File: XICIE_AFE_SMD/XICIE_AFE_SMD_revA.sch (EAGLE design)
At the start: 21 parts, among them IC1 LM324D, IC2 CY8C4245T, IC3 AAT1217, J1 22-27-2021-02, Q1 MOSFET-NCHANNELBSS123LT1G, Q2 MOSFET-NCHANNELBSS123LT1G

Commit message: Trying to merge display
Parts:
- removed R8: 1.02 M, rcl:R-EU_R0805
- removed R9: 604 K, rcl:R-EU_R0603
- added C4, C5, C6, C7: 1 uF, rcl:C-EUC0402
- added C8: 2.2 uF, rcl:C-EUC0603
- added C9: 4.7 uF, rcl:C-EUC0603
- added R5: 390K, resistor:R-EU_R0603
- added U$2: ER-OLED0.96, juliano:ER-OLED0.96
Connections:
- removed net N$14: IC3.FB, R8.2, R9.1
- new net C1N: C4.1, U$2G$5.1
- new net C1P: C4.2, U$2G$4.1
- new net C2N: C5.1, U$2G$3.1
- new net C2P: C5.2, U$2G$2.1
- new net CS#: U$2G$13.1
- new net D/C#: U$2G$15.1
- new net D0: U$2G$18.1
- new net D1: U$2G$19.1
- new net D2: U$2G$20.1
- new net D3: U$2G$21.1
- new net D4: U$2G$22.1
- new net D5: U$2G$23.1
- new net D6: U$2G$24.1
- new net D7: U$2G$25.1
- new net E/RD#: U$2G$17.1
- new net IREF: R5.1, U$2G$26.1
- new net N.C.: U$2G$7.1
- new net R/W#: U$2G$16.1
- new net RES#: U$2G$14.1
- new net V+: C6.1, U$2G$6.1
- new net V2.1: C9.1, U$2G$27.1
- new net VCC_DISPLAY: C8.1, U$2G$28.1
- new net VDD: C7.1, U$2G$11.1, U$2G$9.1
- net GND: now also C6.2, C7.2, C8.2, C9.2, R5.2, U$2G$1.1, U$2G$10.1, U$2G$12.1, U$2G$29.1, U$2G$30.1, U$2G$8.1; no longer R9.2
- net VCC: no longer R8.1
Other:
- note added: "1.65 - 3.3"
- note added: "3.5 - 4.2"
- note added: "BS0"
- note added: "BS1"
- note added: "BS2"
- note added: "Fixed Voltage Must be unconnected"
- note added: "N.C.(GND)"
- note added: "VBAT"
- note added: "VCOMH"
- note added: "VLSS"
- note added: "VSS"

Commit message: Intermediate commit to change computers...
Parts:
- added R7: 1.02 M, rcl:R-EU_R0805
- added R8: 604 k, rcl:R-EU_R0603
- added R9: 150 k, rcl:R-EU_R0603
- added U$3: AAT3221, juliano:AAT3221
- added U$4: MMA7660FC, juliano:MMA7660FC
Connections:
- removed net D0: U$2G$18.1
- removed net D1: U$2G$19.1
- removed net D2: U$2G$20.1
- removed net V+: C6.1, U$2G$6.1
- removed net VDD: C7.1, U$2G$11.1, U$2G$9.1
- new net +3V3: C3.1, C6.1, D1.C, IC1P.V+, IC2.VDDDA, IC3.VOUT, R2.2, R3.2, R7.1, R9.1, U$1.C, U$2G$6.1, U$3.IN, U$4.AVDD
- new net N$12: IC3.FB, R7.2, R8.1
- new net N$14: R9.2, U$3.EN
- new net SCL: U$2G$18.1, U$4.SCL
- new net SDA: U$2G$19.1, U$2G$20.1, U$4.SDA
- net GND: now also R8.2, U$3.GND, U$4.AVSS, U$4.DVSS, U$4.RESERVED(GND)
- net VCC: now also C7.1, IC2.VCCD, IC2.VDDD(19), IC2.VDDD(34), U$2G$11.1, U$2G$9.1, U$3.OUT, U$4.DVDD; no longer C3.1, D1.C, IC1P.V+, IC2.VDDDA, IC3.VOUT, R2.2, R3.2, U$1.C
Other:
- note added: "1.8V"
- note added: "D0"
- note added: "D1"
- note added: "D2"
- note added: "RECALCULAR"
- note added: "SA0"
- note added: "SCL"
- note added: "SDA"
- note added: "VDD"
- note removed: "Fixed Voltage Must be unconnected"
- moved on the sheet: C3, R4

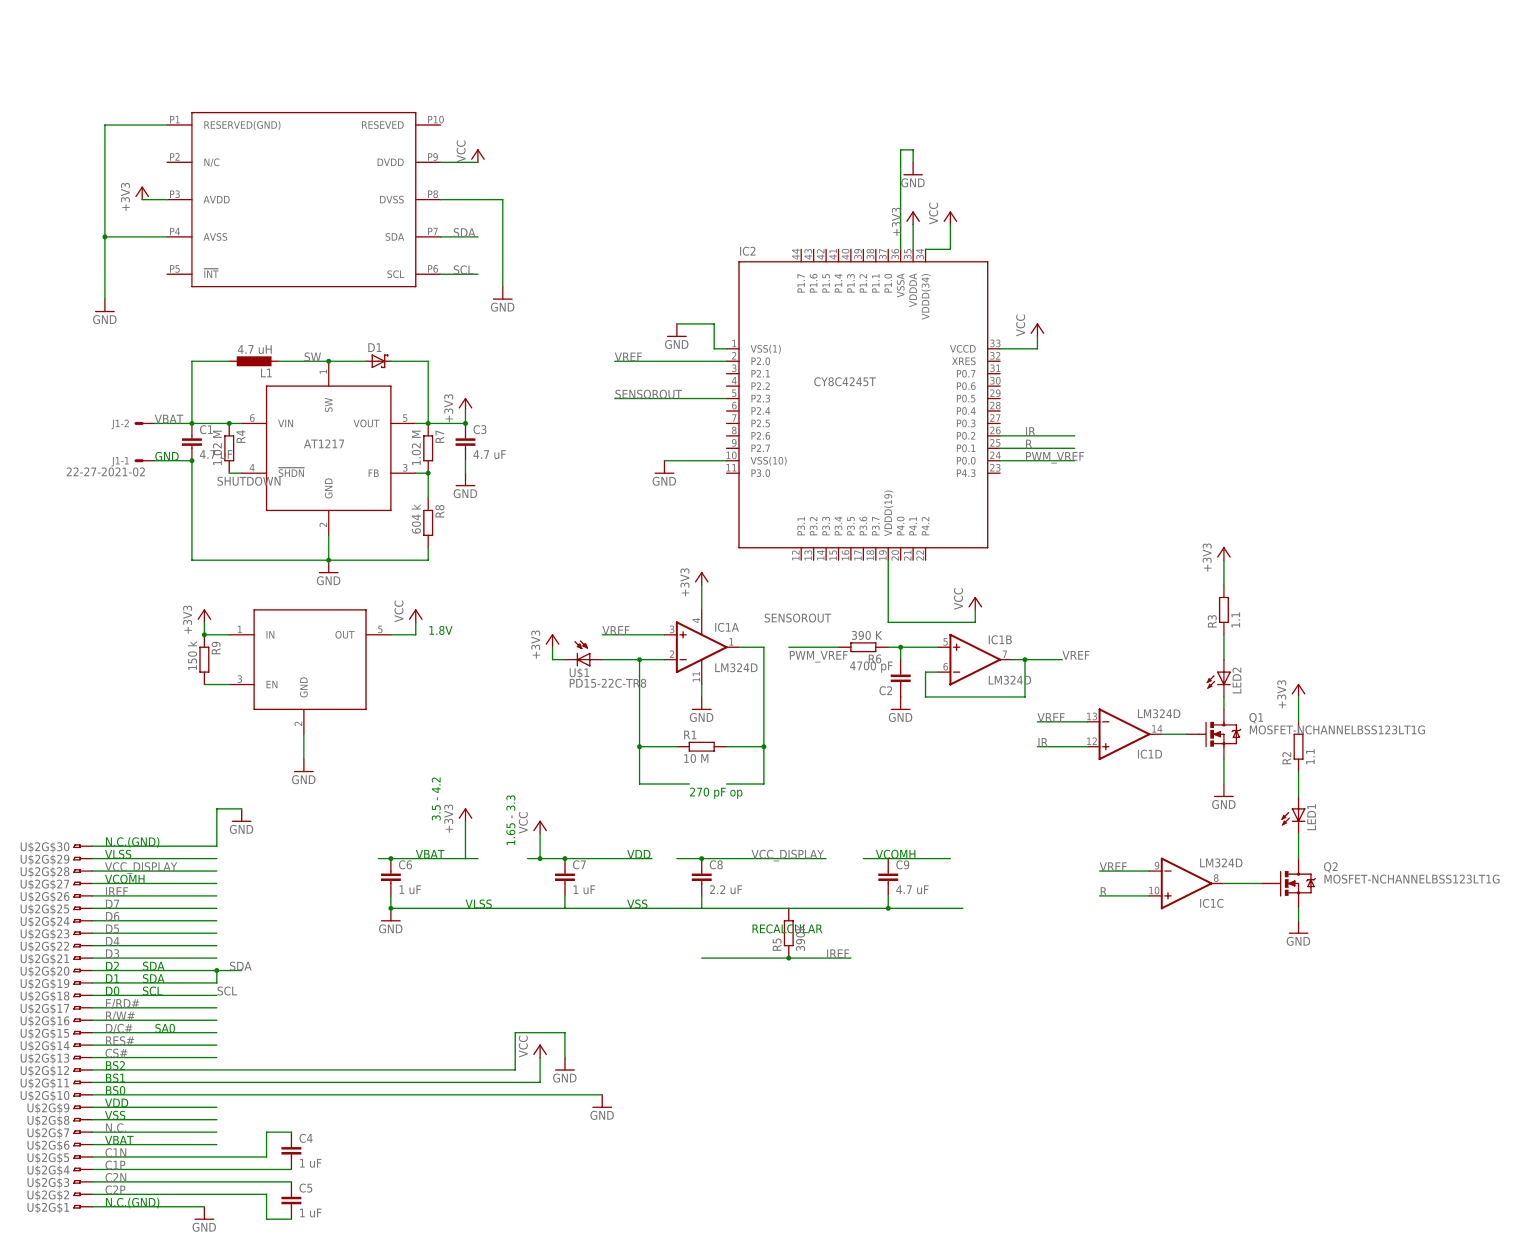
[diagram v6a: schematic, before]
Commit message: Added all components and connections
Still in doubt if BUZZ driver will use a resistor,
and if TIA should have a capacitor.
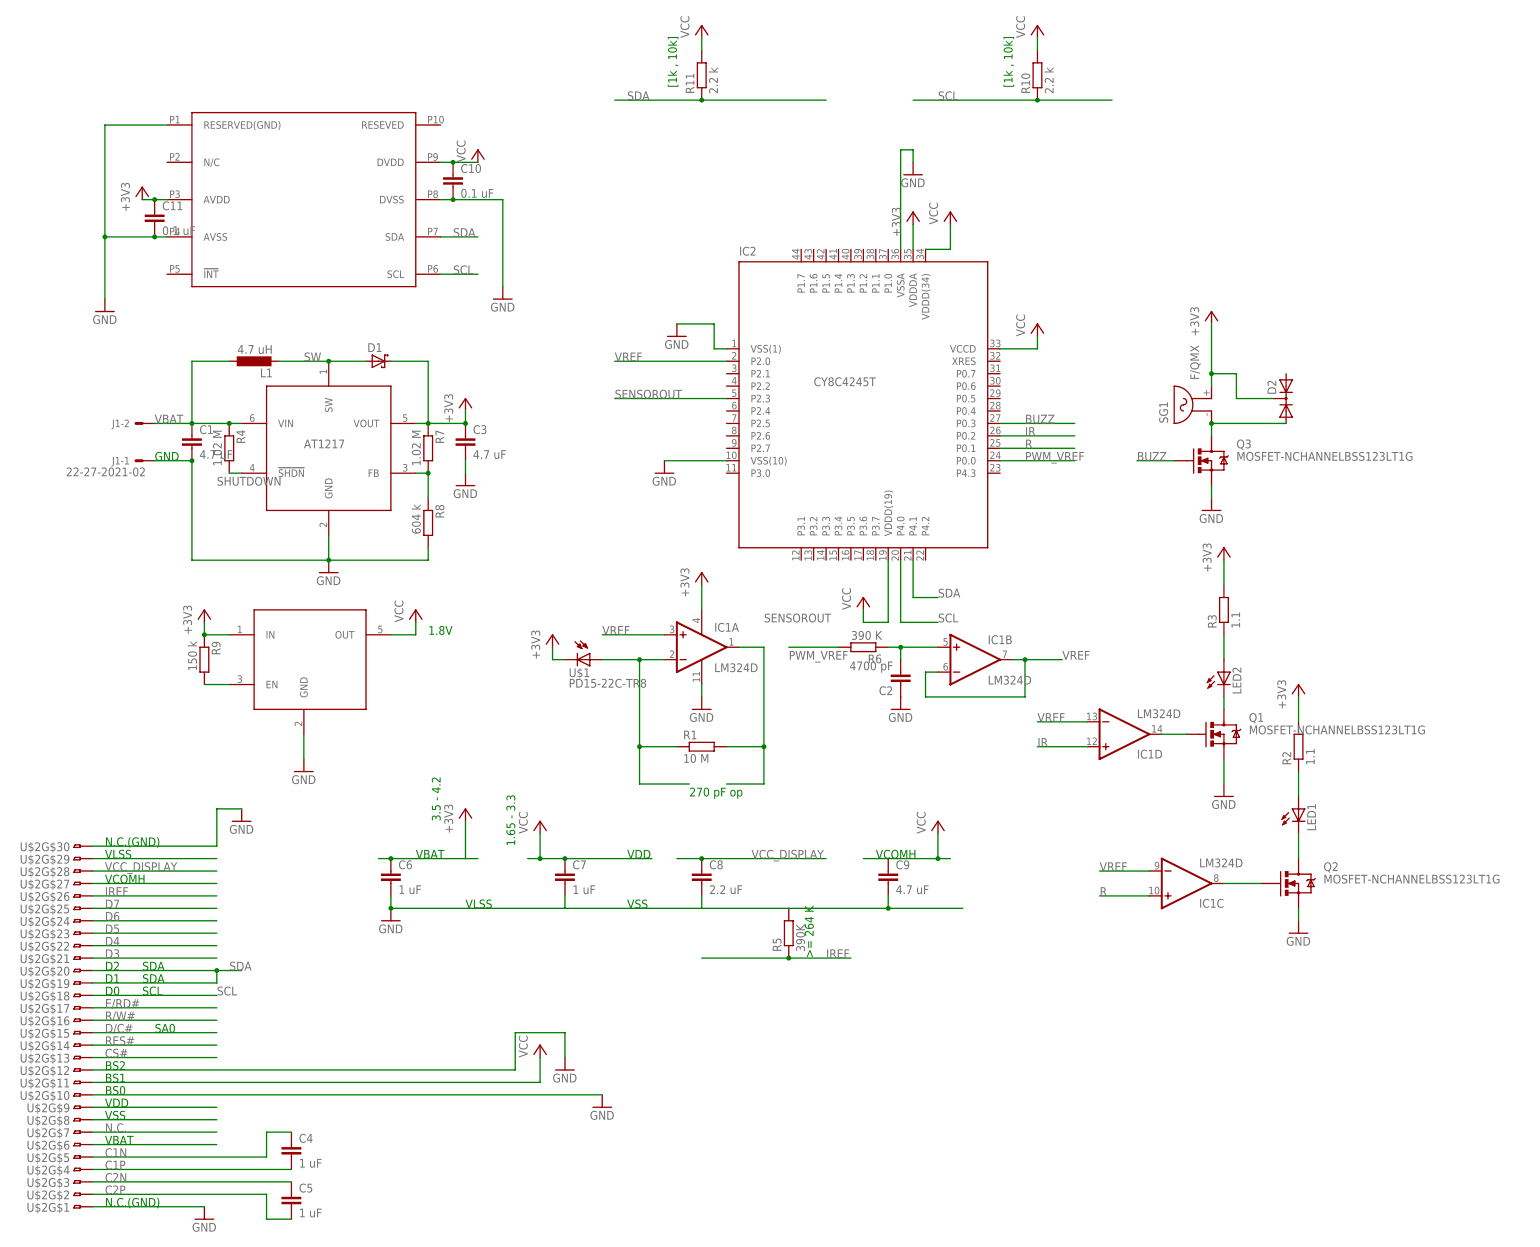
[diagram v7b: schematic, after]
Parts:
- added C10, C11: 0.1 uF, rcl:C-EUC0402
- added D2: (no value), diode:DIODE-2AC|CASOT23
- added Q3: MOSFET-NCHANNELBSS123LT1G, SparkFun-DiscreteSemi:MOSFET-NCHANNELBSS123LT1G
- added R10, R11: 2.2 k, rcl:R-EU_R0402
- added SG1: F/QMX, buzzer:F/QMX
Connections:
- removed net V2.1: C9.1, U$2G$27.1
- new net BUZZ: IC2.P0.3, Q3.G
- new net N$13: D2.A1, Q3.D, SG1.1
- net +3V3: now also C11.1, D2.C, SG1.2
- net GND: now also C10.2, C11.2, Q3.S
- net SCL: now also IC2.P4.0, R10.1
- net SDA: now also IC2.P4.1, R11.1
- net VCC: now also C10.1, C9.1, R10.2, R11.2, U$2G$27.1
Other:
- note added: "[1k , 10k]"
- note removed: "RECALCULAR"
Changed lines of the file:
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@@
 <?xml version="1.0" encoding="utf-8"?>
 <!DOCTYPE eagle SYSTEM "eagle.dtd">
-<eagle version="6.4">
+<eagle version="6.5.0">
 <drawing>
 <settings>
@@
 <part name="+3V9" library="supply1" deviceset="+3V3" device=""/>
 <part name="P+5" library="supply1" deviceset="VCC" device=""/>
+<part name="P+8" library="supply1" deviceset="VCC" device=""/>
+<part name="P+9" library="supply1" deviceset="VCC" device=""/>
+<part name="R10" library="rcl" deviceset="R-EU_" device="R0402" value="2.2 k"/>
+<part name="R11" library="rcl" deviceset="R-EU_" device="R0402" value="2.2 k"/>
+<part name="P+10" library="supply1" deviceset="VCC" device=""/>
+<part name="C10" library="rcl" deviceset="C-EU" device="C0402" value="0.1 uF"/>
+<part name="C11" library="rcl" deviceset="C-EU" device="C0402" value="0.1 uF"/>
+<part name="SG1" library="buzzer" deviceset="F/QMX" device=""/>
+<part name="Q3" library="SparkFun-DiscreteSemi" deviceset="MOSFET-NCHANNEL" device="BSS123LT1G"/>
+<part name="+3V10" library="supply1" deviceset="+3V3" device=""/>
+<part name="GND18" library="supply1" deviceset="GND" device=""/>
+<part name="D2" library="diode" deviceset="DIODE-2AC|CA" device="SOT23"/>
 </parts>
 <sheets>
@@
 <text x="-88.9" y="20.32" size="1.778" layer="91">D1</text>
 <text x="-88.9" y="22.86" size="1.778" layer="91">D2</text>
-<text x="43.18" y="30.48" size="1.778" layer="91">RECALCULAR</text>
+<text x="55.88" y="25.4" size="1.778" layer="91" rot="R90">&gt;= 264 K</text>
+<text x="96.52" y="203.2" size="1.778" layer="91" rot="R90">[1k , 10k]</text>
+<text x="27.94" y="203.2" size="1.778" layer="91" rot="R90">[1k , 10k]</text>
 </plain>
 <instances>
@@
 <instance part="P+2" gate="VCC" x="0" y="7.62"/>
 <instance part="+3V7" gate="G$1" x="-15.24" y="55.88"/>
-<instance part="P+3" gate="VCC" x="88.9" y="99.06"/>
+<instance part="P+3" gate="VCC" x="66.04" y="99.06"/>
 <instance part="P+4" gate="VCC" x="101.6" y="154.94"/>
 <instance part="P+7" gate="VCC" x="83.82" y="177.8"/>
@@
 <instance part="+3V9" gate="G$1" x="-81.28" y="182.88"/>
 <instance part="P+5" gate="VCC" x="-12.7" y="190.5"/>
+<instance part="P+8" gate="VCC" x="33.02" y="215.9"/>
+<instance part="P+9" gate="VCC" x="101.6" y="215.9"/>
+<instance part="R10" gate="G$1" x="101.6" y="205.74" rot="R90"/>
+<instance part="R11" gate="G$1" x="33.02" y="205.74" rot="R90"/>
+<instance part="P+10" gate="VCC" x="81.28" y="53.34"/>
+<instance part="C10" gate="G$1" x="-17.78" y="185.42"/>
+<instance part="C11" gate="G$1" x="-78.74" y="177.8"/>
+<instance part="SG1" gate="G$1" x="134.62" y="137.16" rot="R90"/>
+<instance part="Q3" gate="G$1" x="137.16" y="127"/>
+<instance part="+3V10" gate="G$1" x="137.16" y="157.48"/>
+<instance part="GND18" gate="1" x="137.16" y="116.84"/>
+<instance part="D2" gate="-B1" x="152.4" y="139.7" rot="R90"/>
 </instances>
 <busses>
@@
 <pinref part="IC2" gate="G$1" pin="VDDD(19)"/>
 <pinref part="P+3" gate="VCC" pin="VCC"/>
-<wire x1="88.9" y1="96.52" x2="88.9" y2="93.98" width="0.1524" layer="91"/>
-<wire x1="88.9" y1="93.98" x2="71.12" y2="93.98" width="0.1524" layer="91"/>
+<wire x1="66.04" y1="96.52" x2="66.04" y2="93.98" width="0.1524" layer="91"/>
+<wire x1="66.04" y1="93.98" x2="71.12" y2="93.98" width="0.1524" layer="91"/>
 <wire x1="71.12" y1="93.98" x2="71.12" y2="106.68" width="0.1524" layer="91"/>
 </segment>
@@
 <pinref part="U$4" gate="G$1" pin="DVDD"/>
 <pinref part="P+5" gate="VCC" pin="VCC"/>
-<wire x1="-12.7" y1="187.96" x2="-20.32" y2="187.96" width="0.1524" layer="91"/>
+<wire x1="-12.7" y1="187.96" x2="-17.78" y2="187.96" width="0.1524" layer="91"/>
+<pinref part="C10" gate="G$1" pin="1"/>
+<wire x1="-17.78" y1="187.96" x2="-20.32" y2="187.96" width="0.1524" layer="91"/>
+<junction x="-17.78" y="187.96"/>
+</segment>
+<segment>
+<pinref part="R10" gate="G$1" pin="2"/>
+<pinref part="P+9" gate="VCC" pin="VCC"/>
+<wire x1="101.6" y1="210.82" x2="101.6" y2="213.36" width="0.1524" layer="91"/>
+</segment>
+<segment>
+<pinref part="R11" gate="G$1" pin="2"/>
+<pinref part="P+8" gate="VCC" pin="VCC"/>
+<wire x1="33.02" y1="210.82" x2="33.02" y2="213.36" width="0.1524" layer="91"/>
+</segment>
+<segment>
+<wire x1="-91.44" y1="40.64" x2="-66.04" y2="40.64" width="0.1524" layer="91"/>
+<pinref part="U$2" gate="G$27" pin="1"/>
+</segment>
+<segment>
+<wire x1="66.04" y1="45.72" x2="71.12" y2="45.72" width="0.1524" layer="91"/>
+<pinref part="C9" gate="G$1" pin="1"/>
+<wire x1="71.12" y1="45.72" x2="81.28" y2="45.72" width="0.1524" layer="91"/>
+<pinref part="P+10" gate="VCC" pin="VCC"/>
+<wire x1="81.28" y1="50.8" x2="81.28" y2="45.72" width="0.1524" layer="91"/>
+<wire x1="81.28" y1="45.72" x2="83.82" y2="45.72" width="0.1524" layer="91"/>
+<junction x="81.28" y="45.72"/>
 </segment>
 </net>
@@
 <pinref part="U$4" gate="G$1" pin="AVSS"/>
 <pinref part="GND16" gate="1" pin="GND"/>
-<wire x1="-76.2" y1="172.72" x2="-88.9" y2="172.72" width="0.1524" layer="91"/>
+<wire x1="-76.2" y1="172.72" x2="-78.74" y2="172.72" width="0.1524" layer="91"/>
+<wire x1="-78.74" y1="172.72" x2="-88.9" y2="172.72" width="0.1524" layer="91"/>
 <wire x1="-88.9" y1="172.72" x2="-88.9" y2="160.02" width="0.1524" layer="91"/>
 <wire x1="-88.9" y1="172.72" x2="-88.9" y2="195.58" width="0.1524" layer="91"/>
@@
 <wire x1="-88.9" y1="195.58" x2="-76.2" y2="195.58" width="0.1524" layer="91"/>
 <junction x="-88.9" y="172.72"/>
+<pinref part="C11" gate="G$1" pin="2"/>
+<junction x="-78.74" y="172.72"/>
 </segment>
 <segment>
@@
 <pinref part="U$4" gate="G$1" pin="DVSS"/>
 <wire x1="-7.62" y1="162.56" x2="-7.62" y2="180.34" width="0.1524" layer="91"/>
-<wire x1="-7.62" y1="180.34" x2="-20.32" y2="180.34" width="0.1524" layer="91"/>
+<wire x1="-7.62" y1="180.34" x2="-17.78" y2="180.34" width="0.1524" layer="91"/>
+<pinref part="C10" gate="G$1" pin="2"/>
+<wire x1="-17.78" y1="180.34" x2="-20.32" y2="180.34" width="0.1524" layer="91"/>
+<junction x="-17.78" y="180.34"/>
+</segment>
+<segment>
+<pinref part="GND18" gate="1" pin="GND"/>
+<pinref part="Q3" gate="G$1" pin="S"/>
+<wire x1="137.16" y1="119.38" x2="137.16" y2="121.92" width="0.1524" layer="91"/>
 </segment>
 </net>
@@
 </segment>
 </net>
-<net name="V2.1" class="0">
-<segment>
-<wire x1="66.04" y1="45.72" x2="71.12" y2="45.72" width="0.1524" layer="91"/>
-<pinref part="C9" gate="G$1" pin="1"/>
-<wire x1="71.12" y1="45.72" x2="83.82" y2="45.72" width="0.1524" layer="91"/>
-</segment>
-<segment>
-<wire x1="-91.44" y1="40.64" x2="-66.04" y2="40.64" width="0.1524" layer="91"/>
-<pinref part="U$2" gate="G$27" pin="1"/>
-</segment>
-</net>
 <net name="VCC_DISPLAY" class="2">
 <segment>
@@
 <pinref part="U$4" gate="G$1" pin="AVDD"/>
 <pinref part="+3V9" gate="G$1" pin="+3V3"/>
-<wire x1="-81.28" y1="180.34" x2="-76.2" y2="180.34" width="0.1524" layer="91"/>
+<wire x1="-81.28" y1="180.34" x2="-78.74" y2="180.34" width="0.1524" layer="91"/>
+<pinref part="C11" gate="G$1" pin="1"/>
+<wire x1="-78.74" y1="180.34" x2="-76.2" y2="180.34" width="0.1524" layer="91"/>
+<junction x="-78.74" y="180.34"/>
+</segment>
+<segment>
+<pinref part="D2" gate="-B1" pin="C"/>
+<wire x1="149.86" y1="139.7" x2="142.24" y2="139.7" width="0.1524" layer="91"/>
+<wire x1="142.24" y1="139.7" x2="142.24" y2="144.78" width="0.1524" layer="91"/>
+<wire x1="142.24" y1="144.78" x2="137.16" y2="144.78" width="0.1524" layer="91"/>
+<pinref part="SG1" gate="G$1" pin="2"/>
+<wire x1="137.16" y1="144.78" x2="137.16" y2="142.24" width="0.1524" layer="91"/>
+<pinref part="+3V10" gate="G$1" pin="+3V3"/>
+<wire x1="137.16" y1="154.94" x2="137.16" y2="144.78" width="0.1524" layer="91"/>
+<junction x="137.16" y="144.78"/>
 </segment>
 </net>
@@
 <junction x="-66.04" y="22.86"/>
 </segment>
+<segment>
+<wire x1="15.24" y1="200.66" x2="33.02" y2="200.66" width="0.1524" layer="91"/>
+<label x="17.78" y="200.66" size="1.778" layer="95"/>
+<pinref part="R11" gate="G$1" pin="1"/>
+<wire x1="33.02" y1="200.66" x2="58.42" y2="200.66" width="0.1524" layer="91"/>
+<junction x="33.02" y="200.66"/>
+</segment>
+<segment>
+<pinref part="IC2" gate="G$1" pin="P4.1"/>
+<wire x1="76.2" y1="106.68" x2="76.2" y2="99.06" width="0.1524" layer="91"/>
+<wire x1="76.2" y1="99.06" x2="81.28" y2="99.06" width="0.1524" layer="91"/>
+<label x="81.28" y="99.06" size="1.778" layer="95"/>
+</segment>
 </net>
 <net name="SCL" class="0">
@@
 <pinref part="U$2" gate="G$18" pin="1"/>
 </segment>
-</net>
+<segment>
+<wire x1="76.2" y1="200.66" x2="101.6" y2="200.66" width="0.1524" layer="91"/>
+<label x="81.28" y="200.66" size="1.778" layer="95"/>
+<pinref part="R10" gate="G$1" pin="1"/>
+<wire x1="101.6" y1="200.66" x2="116.84" y2="200.66" width="0.1524" layer="91"/>
+<junction x="101.6" y="200.66"/>
+</segment>
+<segment>
+<pinref part="IC2" gate="G$1" pin="P4.0"/>
+<wire x1="73.66" y1="106.68" x2="73.66" y2="93.98" width="0.1524" layer="91"/>
+<wire x1="73.66" y1="93.98" x2="81.28" y2="93.98" width="0.1524" layer="91"/>
+<label x="81.28" y="93.98" size="1.778" layer="95"/>
+</segment>
+</net>
+<net name="N$13" class="0">
+<segment>
+<pinref part="Q3" gate="G$1" pin="D"/>
+<pinref part="SG1" gate="G$1" pin="1"/>
+<wire x1="137.16" y1="132.08" x2="137.16" y2="134.62" width="0.1524" layer="91"/>
+<pinref part="D2" gate="-B1" pin="A1"/>
+<wire x1="137.16" y1="134.62" x2="152.4" y2="134.62" width="0.1524" layer="91"/>
+<junction x="137.16" y="134.62"/>
+</segment>
+</net>
+<net name="BUZZ" class="0">
+<segment>
+<pinref part="IC2" gate="G$1" pin="P0.3"/>
+<wire x1="93.98" y1="134.62" x2="109.22" y2="134.62" width="0.1524" layer="91"/>
+<label x="99.06" y="134.62" size="1.778" layer="95"/>
+</segment>
+<segment>
+<pinref part="Q3" gate="G$1" pin="G"/>
+<wire x1="121.92" y1="127" x2="129.54" y2="127" width="0.1524" layer="91"/>
+<label x="121.92" y="127" size="1.778" layer="95"/>
+</segment>
+</net>
